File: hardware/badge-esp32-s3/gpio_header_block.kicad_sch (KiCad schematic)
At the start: 1 part, among them U20 2x14_female

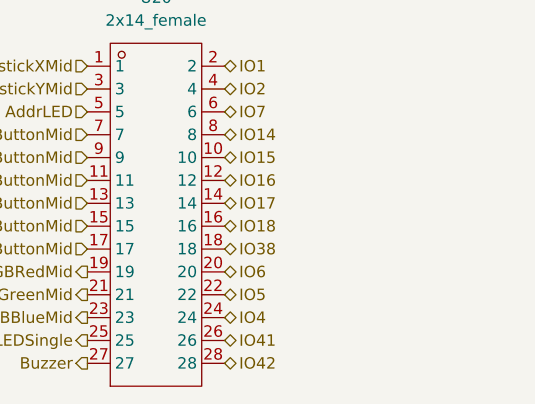
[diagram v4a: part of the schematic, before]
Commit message: added sdio
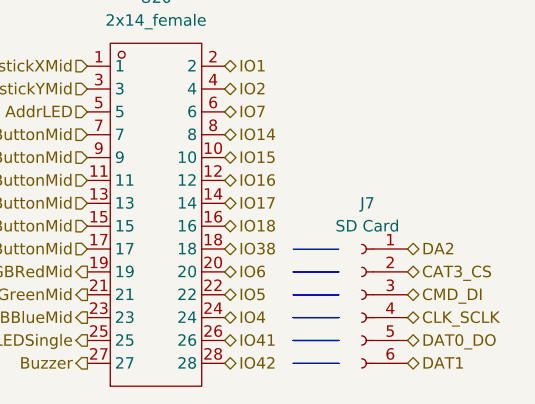
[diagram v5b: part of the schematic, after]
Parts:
- added J7: SD Card, symbol Connector:Conn_01x06_Socket
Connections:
- new net CAT3_CS: J7.2 (Pin_2)
- new net CLK_SCLK: J7.4 (Pin_4)
- new net CMD_DI: J7.3 (Pin_3)
- new net DA2: J7.1 (Pin_1)
- new net DAT0_DO: J7.5 (Pin_5)
- new net DAT1: J7.6 (Pin_6)
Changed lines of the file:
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@@
 	(generator_version "9.0")
 	(paper "A4")
+	(polyline
+		(pts
+			(xy 144.78 100.33) (xy 149.86 100.33)
+		)
+		(stroke
+			(width 0)
+			(type default)
+		)
+	)
+	(polyline
+		(pts
+			(xy 144.78 105.41) (xy 149.86 105.41)
+		)
+		(stroke
+			(width 0)
+			(type default)
+		)
+	)
+	(polyline
+		(pts
+			(xy 144.78 100.33) (xy 149.86 100.33)
+		)
+		(stroke
+			(width 0)
+			(type default)
+		)
+	)
+	(polyline
+		(pts
+			(xy 144.78 102.87) (xy 149.86 102.87)
+		)
+		(stroke
+			(width 0)
+			(type default)
+		)
+	)
+	(polyline
+		(pts
+			(xy 144.78 97.79) (xy 149.86 97.79)
+		)
+		(stroke
+			(width 0)
+			(type default)
+		)
+	)
+	(polyline
+		(pts
+			(xy 144.78 105.41) (xy 149.86 105.41)
+		)
+		(stroke
+			(width 0)
+			(type default)
+		)
+	)
+	(polyline
+		(pts
+			(xy 144.78 107.95) (xy 149.86 107.95)
+		)
+		(stroke
+			(width 0)
+			(type default)
+		)
+	)
+	(polyline
+		(pts
+			(xy 144.78 102.87) (xy 149.86 102.87)
+		)
+		(stroke
+			(width 0)
+			(type default)
+		)
+	)
+	(polyline
+		(pts
+			(xy 144.78 97.79) (xy 149.86 97.79)
+		)
+		(stroke
+			(width 0)
+			(type default)
+		)
+	)
+	(polyline
+		(pts
+			(xy 144.78 107.95) (xy 149.86 107.95)
+		)
+		(stroke
+			(width 0)
+			(type default)
+		)
+	)
+	(polyline
+		(pts
+			(xy 144.78 95.25) (xy 149.86 95.25)
+		)
+		(stroke
+			(width 0)
+			(type default)
+		)
+	)
+	(hierarchical_label "DAT0_DO"
+		(shape bidirectional)
+		(at 157.48 105.41 0)
+		(effects
+			(font
+				(size 1.27 1.27)
+			)
+			(justify left)
+		)
+	)
+	(hierarchical_label "CMD_DI"
+		(shape bidirectional)
+		(at 157.48 100.33 0)
+		(effects
+			(font
+				(size 1.27 1.27)
+			)
+			(justify left)
+		)
+	)
 	(hierarchical_label "IO1"
 		(shape bidirectional)
@@
 		(shape bidirectional)
 		(at 137.16 77.47 0)
+		(effects
+			(font
+				(size 1.27 1.27)
+			)
+			(justify left)
+		)
+	)
+	(hierarchical_label "CAT3_CS"
+		(shape bidirectional)
+		(at 157.48 97.79 0)
 		(effects
 			(font
@@
 		)
 	)
+	(hierarchical_label "DA2"
+		(shape bidirectional)
+		(at 157.48 95.25 0)
+		(effects
+			(font
+				(size 1.27 1.27)
+			)
+			(justify left)
+		)
+	)
 	(hierarchical_label "IO7"
 		(shape bidirectional)
@@
 		)
 	)
+	(hierarchical_label "DAT1"
+		(shape bidirectional)
+		(at 157.48 107.95 0)
+		(effects
+			(font
+				(size 1.27 1.27)
+			)
+			(justify left)
+		)
+	)
+	(hierarchical_label "CLK_SCLK"
+		(shape bidirectional)
+		(at 157.48 102.87 0)
+		(effects
+			(font
+				(size 1.27 1.27)
+			)
+			(justify left)
+		)
+	)
 	(hierarchical_label "JoystickXMid"
 		(shape input)
@@
 		)
 	)
+	(symbol
+		(lib_id "Connector:Conn_01x06_Socket")
+		(at 152.4 100.33 0)
+		(mirror y)
+		(unit 1)
+		(exclude_from_sim no)
+		(in_bom yes)
+		(on_board yes)
+		(dnp no)
+		(fields_autoplaced yes)
+		(property "Reference" "J7"
+			(at 153.035 90.17 0)
+			(effects
+				(font
+					(size 1.27 1.27)
+				)
+			)
+		)
+		(property "Value" "SD Card"
+			(at 153.035 92.71 0)
+			(effects
+				(font
+					(size 1.27 1.27)
+				)
+			)
+		)
+		(property "Footprint" ""
+			(at 152.4 100.33 0)
+			(effects
+				(font
+					(size 1.27 1.27)
+				)
+				(hide yes)
+			)
+		)
+		(property "Datasheet" "~"
+			(at 152.4 100.33 0)
+			(effects
+				(font
+					(size 1.27 1.27)
+				)
+				(hide yes)
+			)
+		)
+		(property "Description" "Generic connector, single row, 01x06, script generated"
+			(at 152.4 100.33 0)
+			(effects
+				(font
+					(size 1.27 1.27)
+				)
+				(hide yes)
+			)
+		)
+		(pin "5"
+		)
+		(pin "1"
+		)
+		(pin "6"
+		)
+		(pin "4"
+		)
+		(pin "2"
+		)
+		(pin "3"
+		)
+		(instances
+			(project "badge-esp32-s3"
+				(path "/e2af9a6c-dbe9-4de2-9ba6-ea213a7300ec/959f77f2-91ca-4227-8718-f4511dce7e9a"
+					(reference "J7")
+					(unit 1)
+				)
+			)
+		)
+	)

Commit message: almost finished
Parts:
- removed J7: SD Card, symbol Connector:Conn_01x06_Socket
- removed U20: 2x14_female, lcsc-lib:HDR-TH_28P-P2.54-V-F-R2-C14-S2.54, symbol lcsc-lib:HX PM2.54-2X14P ZC
- added J4: Conn_02x15_Odd_Even, Connector_PinHeader_2.54mm:PinHeader_2x15_P2.54mm_Vertical, symbol Connector_Generic:Conn_02x15_Odd_Even
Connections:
- net AButtonMid: now also J4.25 (Pin_25)
- net AddrLED: now also J4.9 (Pin_9)
- net BButtonMid: now also J4.23 (Pin_23)
- net Buzzer: now also J4.27 (Pin_27)
- net DownButtonMid: now also J4.21 (Pin_21)
- net IO1: now also J4.2 (Pin_2)
- net IO14: now also J4.8 (Pin_8)
- net IO15: now also J4.10 (Pin_10)
- net IO16: now also J4.12 (Pin_12)
- net IO17: now also J4.14 (Pin_14)
- net IO18: now also J4.16 (Pin_16)
- net IO2: now also J4.4 (Pin_4)
- net IO38: now also J4.18 (Pin_18)
- net IO4: now also J4.24 (Pin_24)
- net IO41: now also J4.26 (Pin_26)
- net IO42: now also J4.28 (Pin_28)
- net IO5: now also J4.22 (Pin_22)
- net IO6: now also J4.20 (Pin_20)
- net IO7: now also J4.6 (Pin_6)
- net JoystickXMid: now also J4.11 (Pin_11)
- net JoystickYMid: now also J4.13 (Pin_13)
- net LEDSingle: now also J4.7 (Pin_7)
- net LeftButtonMid: now also J4.19 (Pin_19)
- net RGBBlueMid: now also J4.5 (Pin_5)
- net RGBGreenMid: now also J4.3 (Pin_3)
- net RGBRedMid: now also J4.1 (Pin_1)
- net RightButtonMid: now also J4.15 (Pin_15)
- net UpButtonMid: now also J4.17 (Pin_17)
- new net BatteryVoltage: J4.29 (Pin_29)
- new net IO43: J4.30 (Pin_30)

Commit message: final changes and part updated
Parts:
- J4: footprint Connector_PinHeader_2.54mm:PinHeader_2x15_P2.54mm_Vertical -> Connector_PinSocket_2.54mm:PinSocket_2x15_P2.54mm_Vertical; LCSC Part C7499350 -> C7500799
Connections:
- net IO1 is gone; now on net RGBRedMid: J4.2 (Pin_2)
- net IO14 is gone; now on net LEDSingle: J4.8 (Pin_8)
- net IO15 is gone; now on net AddrLED: J4.10 (Pin_10)
- net IO16 is gone; now on net JoystickXMid: J4.12 (Pin_12)
- net IO17 is gone; now on net JoystickYMid: J4.14 (Pin_14)
- net IO18 is gone; now on net RightButtonMid: J4.16 (Pin_16)
- net IO38 is gone; now on net UpButtonMid: J4.18 (Pin_18)
- net IO41 is gone; now on net AButtonMid: J4.26 (Pin_26)
- net IO42 is gone; now on net Buzzer: J4.28 (Pin_28)
- net IO43 is gone; now on net BatteryVoltage: J4.30 (Pin_30)
- net AButtonMid: no longer J4.25 (Pin_25)
- net AddrLED: no longer J4.9 (Pin_9)
- net BButtonMid: now also J4.24 (Pin_24); no longer J4.23 (Pin_23)
- net BatteryVoltage: no longer J4.29 (Pin_29)
- net Buzzer: no longer J4.27 (Pin_27)
- net DownButtonMid: now also J4.22 (Pin_22); no longer J4.21 (Pin_21)
- net IO2: now also J4.1 (Pin_1); no longer J4.4 (Pin_4)
- net IO4: now also J4.3 (Pin_3); no longer J4.24 (Pin_24)
- net IO5: now also J4.5 (Pin_5); no longer J4.22 (Pin_22)
- net IO6: now also J4.7 (Pin_7); no longer J4.20 (Pin_20)
- net IO7: now also J4.9 (Pin_9); no longer J4.6 (Pin_6)
- net JoystickXMid: no longer J4.11 (Pin_11)
- net JoystickYMid: no longer J4.13 (Pin_13)
- net LEDSingle: no longer J4.7 (Pin_7)
- net LeftButtonMid: now also J4.20 (Pin_20); no longer J4.19 (Pin_19)
- net RGBBlueMid: now also J4.6 (Pin_6); no longer J4.5 (Pin_5)
- net RGBGreenMid: now also J4.4 (Pin_4); no longer J4.3 (Pin_3)
- net RGBRedMid: no longer J4.1 (Pin_1)
- net RightButtonMid: no longer J4.15 (Pin_15)
- net UpButtonMid: no longer J4.17 (Pin_17)
- new net IO10: J4.15 (Pin_15)
- new net IO11: J4.17 (Pin_17)
- new net IO12: J4.29 (Pin_29)
- new net IO21: J4.19 (Pin_19)
- new net IO33: J4.23 (Pin_23)
- new net IO34: J4.25 (Pin_25)
- new net IO47: J4.21 (Pin_21)
- new net IO48: J4.27 (Pin_27)
- new net IO8: J4.11 (Pin_11)
- new net IO9: J4.13 (Pin_13)

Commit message: finished component alignment
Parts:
- J4: FT Rotation Offset (none) -> -90; LCSC Part C7500799 -> C7499350
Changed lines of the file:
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@@
 			)
 		)
-		(property "LCSC Part" "C7500799"
+		(property "LCSC Part" "C7499350"
 			(at 109.22 140.97 0)
 			(effects
+				(font
+					(size 1.27 1.27)
+				)
+				(hide yes)
+			)
+		)
+		(property "FT Rotation Offset" "-90"
+			(at 109.22 140.97 0)
+			(effects
